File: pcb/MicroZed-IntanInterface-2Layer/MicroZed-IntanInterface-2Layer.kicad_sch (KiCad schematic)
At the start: 51 parts, among them J1 Screw_Terminal_01x02, J2 Conn_02x05_Odd_Even, J4 USB_C_Receptacle_USB2.0_16P, J7 GND header for probes, U1 AP331A, U2 TLV62568DDC, U9 TLV62568DDC

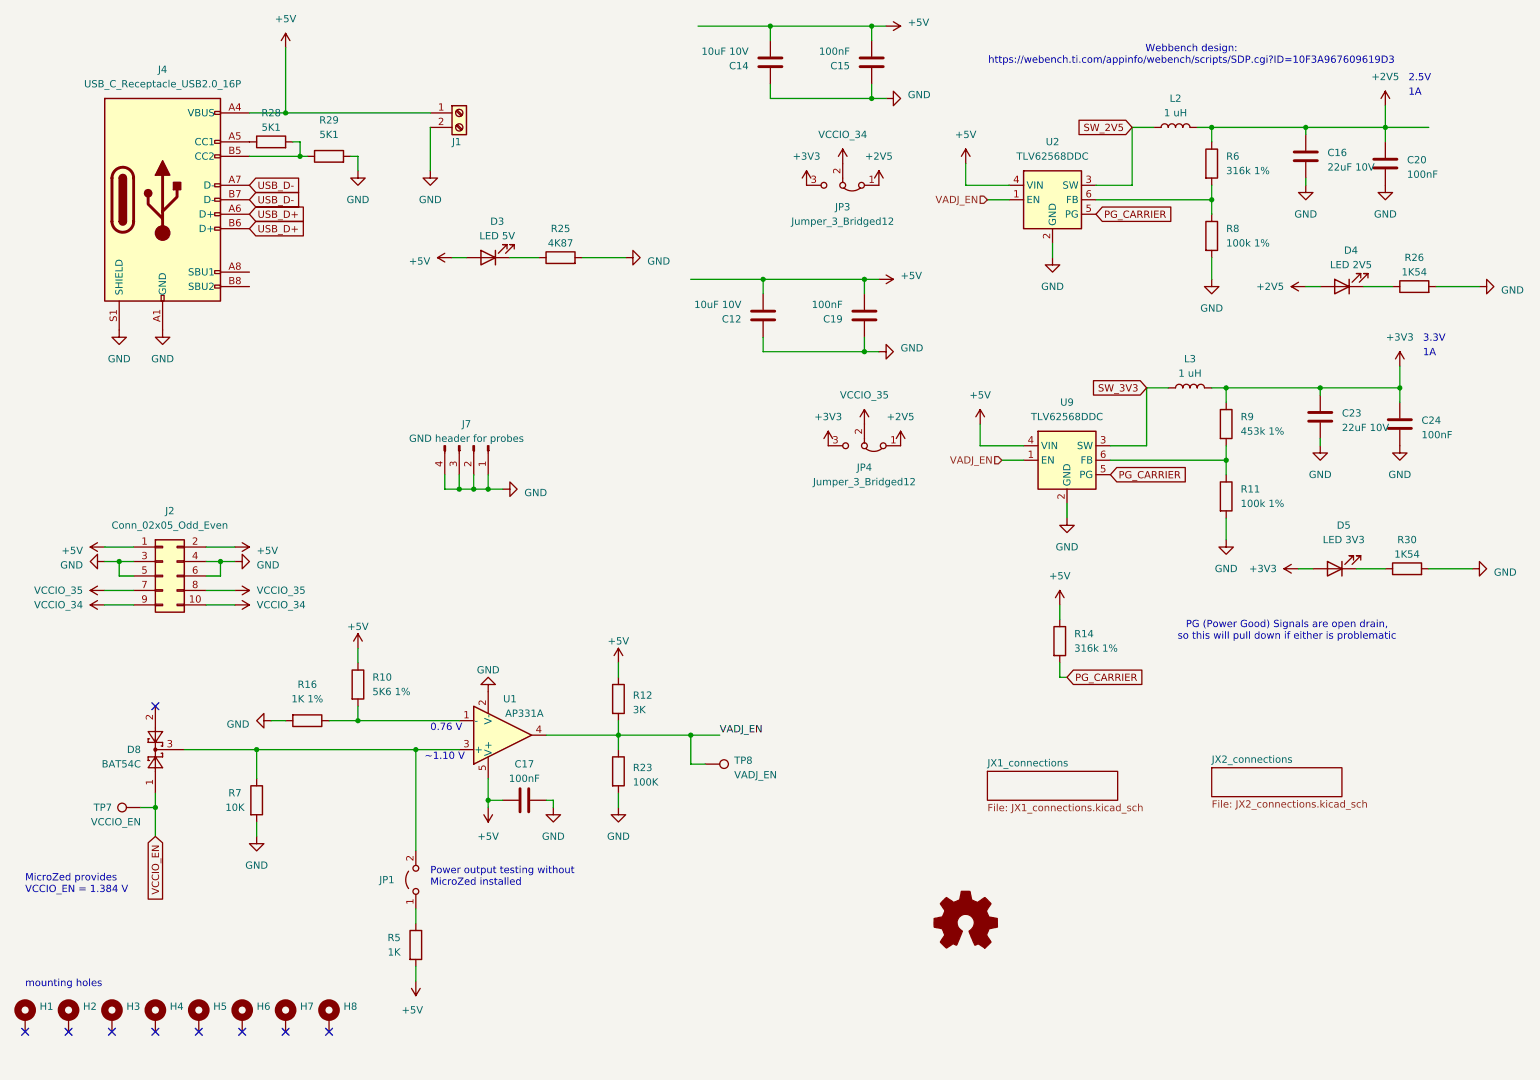
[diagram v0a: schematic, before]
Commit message: Updated PCB after v0.22 bug fixes
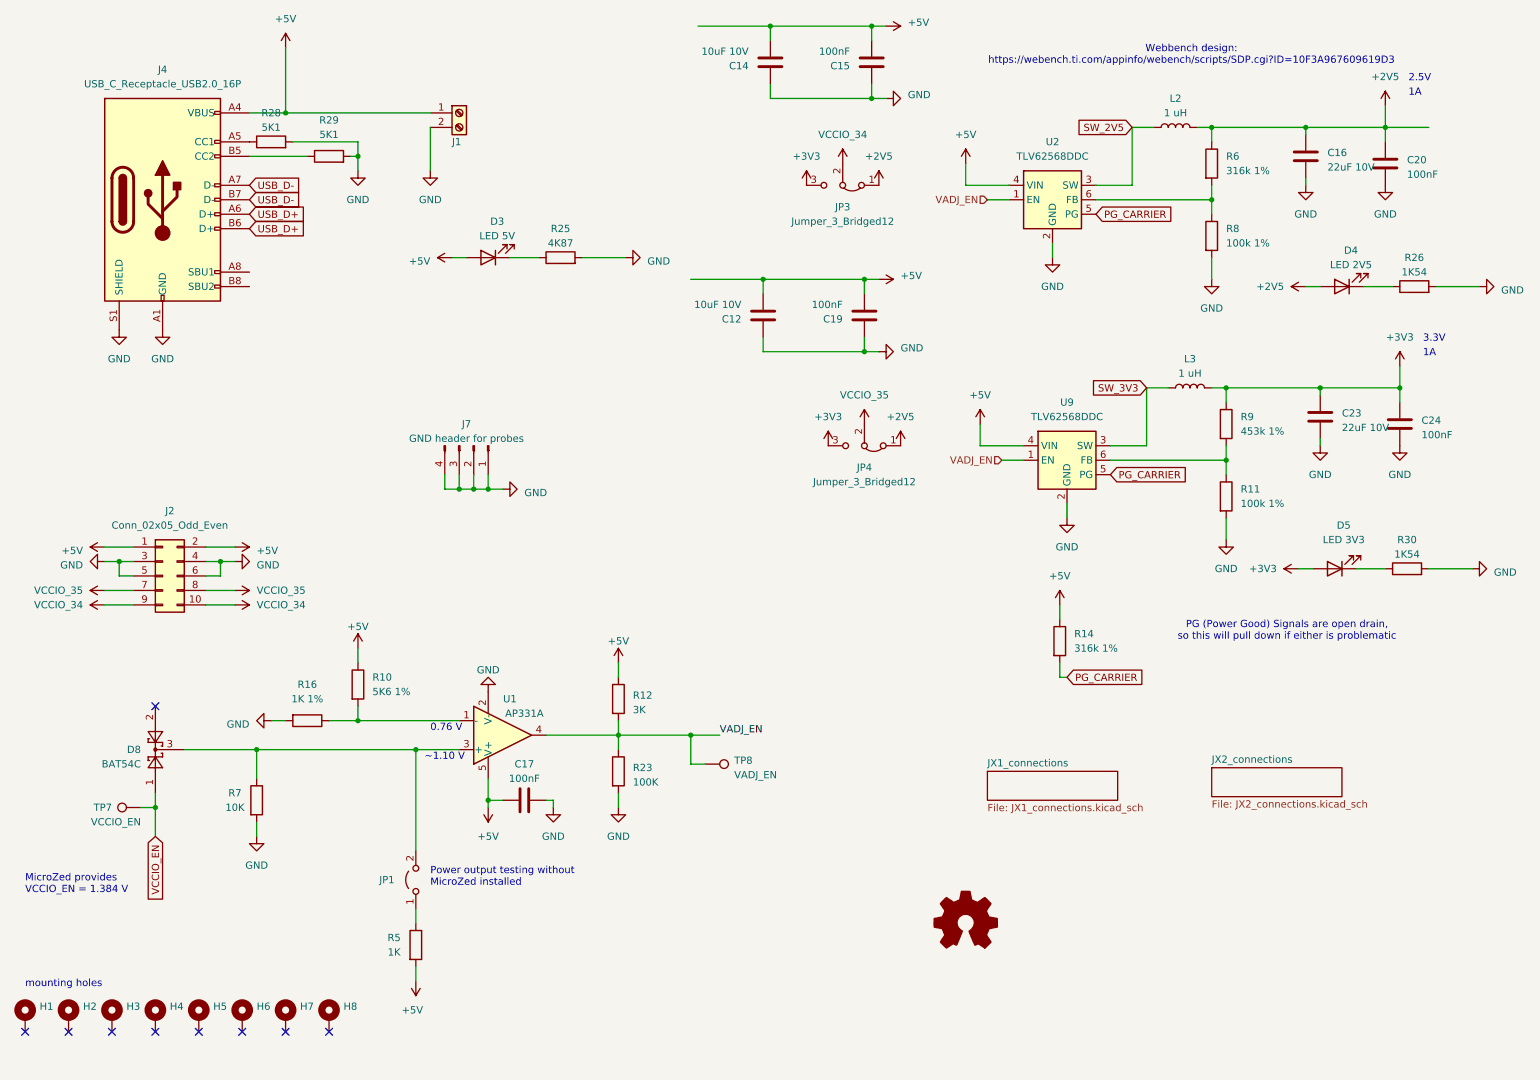
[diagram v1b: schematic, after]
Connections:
- net GND: now also R28.2
- net at J4.B5 (CC2), R29.1: no longer R28.2
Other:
- title: MicroZed development carrier board -> Intan Interface carrier board
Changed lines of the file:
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@@
 (kicad_sch
-	(version 20231120)
+	(version 20250114)
 	(generator "eeschema")
-	(generator_version "8.0")
+	(generator_version "9.0")
 	(paper "A4")
 	(title_block
-		(title "MicroZed development carrier board")
-		(date "2023-08-19")
-		(rev "4")
+		(title "Intan Interface carrier board")
+		(date "2025-08-18")
+		(rev "1.0")
 		(comment 1 "               License: Creative Commons Zero")
-		(comment 3 "               (c) 2023 Viktor Nikolov")
+		(comment 3 "               (c) 2025 Caleb Kemere")
+		(comment 4 "                    derived from a design by  Viktor Nikolov")
+	)
+	(text "1A"
+		(exclude_from_sim no)
+		(at 263.144 28.956 0)
+		(effects
+			(font
+				(size 1.27 1.27)
+			)
+			(justify left bottom)
+		)
+	)
+	(text "3.3V"
+		(exclude_from_sim no)
+		(at 265.684 72.136 0)
+		(effects
+			(font
+				(size 1.27 1.27)
+			)
+			(justify left bottom)
+		)
+	)
+	(text "mounting holes"
+		(exclude_from_sim no)
+		(at 20.32 185.42 0)
+		(effects
+			(font
+				(size 1.27 1.27)
+			)
+			(justify left bottom)
+		)
+	)
+	(text "2.5V"
+		(exclude_from_sim no)
+		(at 263.144 26.416 0)
+		(effects
+			(font
+				(size 1.27 1.27)
+			)
+			(justify left bottom)
+		)
+	)
+	(text "0.76 V"
+		(exclude_from_sim no)
+		(at 91.44 140.462 0)
+		(effects
+			(font
+				(size 1.27 1.27)
+			)
+			(justify left bottom)
+		)
+	)
+	(text "Webbench design:\nhttps://webench.ti.com/appinfo/webench/scripts/SDP.cgi?ID=10F3A967609619D3"
+		(exclude_from_sim no)
+		(at 225.044 21.59 0)
+		(effects
+			(font
+				(size 1.27 1.27)
+			)
+		)
+	)
+	(text "~1.10 V"
+		(exclude_from_sim no)
+		(at 90.424 145.542 0)
+		(effects
+			(font
+				(size 1.27 1.27)
+			)
+			(justify left bottom)
+		)
+	)
+	(text "Power output testing without\nMicroZed installed"
+		(exclude_from_sim no)
+		(at 91.44 167.64 0)
+		(effects
+			(font
+				(size 1.27 1.27)
+			)
+			(justify left bottom)
+		)
+	)
+	(text "1A"
+		(exclude_from_sim no)
+		(at 265.684 74.676 0)
+		(effects
+			(font
+				(size 1.27 1.27)
+			)
+			(justify left bottom)
+		)
+	)
+	(text "MicroZed provides\nVCCIO_EN = 1.384 V"
+		(exclude_from_sim no)
+		(at 20.32 168.91 0)
+		(effects
+			(font
+				(size 1.27 1.27)
+			)
+			(justify left bottom)
+		)
+	)
+	(text "PG (Power Good) Signals are open drain, \nso this will pull down if either is problematic\n"
+		(exclude_from_sim no)
+		(at 241.808 122.682 0)
+		(effects
+			(font
+				(size 1.27 1.27)
+			)
+		)
 	)
 	(junction
@@
 	)
 	(junction
+		(at 78.74 39.37)
+		(diameter 0)
+		(color 0 0 0 0)
+	)
+	(junction
 		(at 88.9 143.51)
 		(diameter 0)
@@
 	)
 	(junction
-		(at 68.58 39.37)
-		(diameter 0)
-		(color 0 0 0 0)
-	)
-	(junction
 		(at 259.08 34.29)
 		(diameter 0)
@@
 	(wire
 		(pts
-			(xy 68.58 36.83) (xy 68.58 39.37)
-		)
-		(stroke
-			(width 0)
-			(type default)
-		)
-	)
-	(wire
-		(pts
 			(xy 36.83 113.03) (xy 39.37 113.03)
 		)
@@
 	(wire
 		(pts
+			(xy 78.74 36.83) (xy 78.74 39.37)
+		)
+		(stroke
+			(width 0)
+			(type default)
+		)
+	)
+	(wire
+		(pts
 			(xy 171.45 29.21) (xy 168.91 29.21)
 		)
@@
 	(wire
 		(pts
-			(xy 67.31 36.83) (xy 68.58 36.83)
+			(xy 67.31 36.83) (xy 78.74 36.83)
 		)
 		(stroke
@@
 	(wire
 		(pts
-			(xy 69.85 39.37) (xy 68.58 39.37)
+			(xy 59.69 39.37) (xy 69.85 39.37)
 		)
 		(stroke
@@
 	(wire
 		(pts
-			(xy 68.58 39.37) (xy 59.69 39.37)
-		)
-		(stroke
-			(width 0)
-			(type default)
-		)
-	)
-	(wire
-		(pts
 			(xy 228.6 60.96) (xy 228.6 57.15)
 		)
@@
 		)
 	)
-	(text "1A"
-		(exclude_from_sim no)
-		(at 263.144 28.956 0)
-		(effects
-			(font
-				(size 1.27 1.27)
-			)
-			(justify left bottom)
-		)
-	)
-	(text "3.3V"
-		(exclude_from_sim no)
-		(at 265.684 72.136 0)
-		(effects
-			(font
-				(size 1.27 1.27)
-			)
-			(justify left bottom)
-		)
-	)
-	(text "mounting holes"
-		(exclude_from_sim no)
-		(at 20.32 185.42 0)
-		(effects
-			(font
-				(size 1.27 1.27)
-			)
-			(justify left bottom)
-		)
-	)
-	(text "2.5V"
-		(exclude_from_sim no)
-		(at 263.144 26.416 0)
-		(effects
-			(font
-				(size 1.27 1.27)
-			)
-			(justify left bottom)
-		)
-	)
-	(text "0.76 V"
-		(exclude_from_sim no)
-		(at 91.44 140.462 0)
-		(effects
-			(font
-				(size 1.27 1.27)
-			)
-			(justify left bottom)
-		)
-	)
-	(text "Webbench design:\nhttps://webench.ti.com/appinfo/webench/scripts/SDP.cgi?ID=10F3A967609619D3"
-		(exclude_from_sim no)
-		(at 225.044 21.59 0)
-		(effects
-			(font
-				(size 1.27 1.27)
-			)
-		)
-	)
-	(text "~1.10 V"
-		(exclude_from_sim no)
-		(at 90.424 145.542 0)
-		(effects
-			(font
-				(size 1.27 1.27)
-			)
-			(justify left bottom)
-		)
-	)
-	(text "Power output testing without\nMicroZed installed"
-		(exclude_from_sim no)
-		(at 91.44 167.64 0)
-		(effects
-			(font
-				(size 1.27 1.27)
-			)
-			(justify left bottom)
-		)
-	)
-	(text "1A"
-		(exclude_from_sim no)
-		(at 265.684 74.676 0)
-		(effects
-			(font
-				(size 1.27 1.27)
-			)
-			(justify left bottom)
-		)
-	)
-	(text "MicroZed provides\nVCCIO_EN = 1.384 V"
-		(exclude_from_sim no)
-		(at 20.32 168.91 0)
-		(effects
-			(font
-				(size 1.27 1.27)
-			)
-			(justify left bottom)
-		)
-	)
-	(text "PG (Power Good) Signals are open drain, \nso this will pull down if either is problematic\n"
-		(exclude_from_sim no)
-		(at 241.808 122.682 0)
-		(effects
-			(font
-				(size 1.27 1.27)
-			)
-		)
-	)
 	(label "VADJ_EN"
 		(at 142.24 140.97 0)
@@
 		(at 189.23 147.32)
 		(size 22.86 5.08)
+		(exclude_from_sim no)
+		(in_bom yes)
+		(on_board yes)
+		(dnp no)
 		(fields_autoplaced yes)
 		(stroke
@@
 		)
 		(instances
-			(project "MicroZed-IntanInterface"
+			(project "MicroZed-IntanInterface-2Layer"
 				(path "/e2973d32-f02d-4cac-9cf4-7229e04d7d6c"
 					(page "2")
@@
 		(at 228.6 146.685)
 		(size 22.86 5.08)
+		(exclude_from_sim no)
+		(in_bom yes)
+		(on_board yes)
+		(dnp no)
 		(fields_autoplaced yes)
 		(stroke
@@
 		)
 		(instances
-			(project "MicroZed-IntanInterface"
+			(project "MicroZed-IntanInterface-2Layer"
 				(path "/e2973d32-f02d-4cac-9cf4-7229e04d7d6c"
 					(page "3")
@@
 		)
 	)
+	(embedded_fonts no)
 )

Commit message: Updates for version 1.0 to ship to UMich
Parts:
- removed JP1: Jumper_2_Open, Connector_PinHeader_2.54mm:PinHeader_1x02_P2.54mm_Vertical, symbol Jumper:Jumper_2_Open
- removed JP3, JP4: Jumper_3_Bridged12, Connector_PinHeader_2.54mm:PinHeader_1x03_P2.54mm_Vertical, symbol Jumper:Jumper_3_Bridged12
- added JP5: SolderJumper_2_Open, Jumper:SolderJumper-2_P1.3mm_Open_RoundedPad1.0x1.5mm, symbol Jumper:SolderJumper_2_Open
- added SW3, SW4: SW_SPDT, Button_Switch_SMD:SW_SPDT_PCM12, symbol Switch:SW_SPDT
- C15, C17, C19, C20, C24: footprint Capacitor_SMD:C_0603_1608Metric -> Capacitor_SMD:C_0402_1005Metric; LCSC C66501 -> C307331
- C16, C23: value 22uF 10V -> 22uF 25V; LCSC C5672 -> C12891
- D3, D4, D5: LCSC C2833058 -> C2286
- H1, H2, H3, H4, H5, H6, H7, H8: footprint Viktor:MountingHole_3.2mm_Pad_7mm -> MountingHole:MountingHole_3.2mm_M3_Pad
- J2: now not fitted; now left out of the parts list
- J4: LCSC (none) -> C5184243
- L2, L3: footprint Inductor_SMD:L_1008_2520Metric -> Inductor_SMD:L_1210_3225Metric; LCSC (none) -> C47492669
- R10: value 5K6 1% -> 5.6k 1%; footprint Resistor_SMD:R_0603_1608Metric -> Resistor_SMD:R_0402_1005Metric; LCSC C22843 -> C25908
- R11, R8: footprint Resistor_SMD:R_0603_1608Metric -> Resistor_SMD:R_0402_1005Metric; LCSC (none) -> C25741
- R12: value 3K -> 3k; footprint Resistor_SMD:R_0603_1608Metric -> Resistor_SMD:R_0402_1005Metric; LCSC C4211 -> C22978
- R14, R6: footprint Resistor_SMD:R_0603_1608Metric -> Resistor_SMD:R_0402_1005Metric; LCSC (none) -> C4338094
- R16: value 1K 1% -> 1k 1%; footprint Resistor_SMD:R_0603_1608Metric -> Resistor_SMD:R_0402_1005Metric; LCSC C23228 -> C11702
- R23: value 100K -> 100k 1%; footprint Resistor_SMD:R_0603_1608Metric -> Resistor_SMD:R_0402_1005Metric; LCSC C25803 -> C25741
- R25: value 4K87 -> 1k 1%; footprint Resistor_SMD:R_0603_1608Metric -> Resistor_SMD:R_0402_1005Metric; LCSC C2097544 -> C11702
- R26, R30: value 1K54 -> 1k 1%; footprint Resistor_SMD:R_0603_1608Metric -> Resistor_SMD:R_0402_1005Metric; LCSC C100784 -> C11702
- R28, R29: value 5K1 -> 5.1k; footprint Resistor_SMD:R_0603_1608Metric -> Resistor_SMD:R_0402_1005Metric; LCSC C2097544 -> C25905
- R5: value 1K -> 1k 1%; footprint Resistor_SMD:R_0603_1608Metric -> Resistor_SMD:R_0402_1005Metric; LCSC C21190 -> C11702
- R7: value 10K -> 10k; footprint Resistor_SMD:R_0603_1608Metric -> Resistor_SMD:R_0402_1005Metric; LCSC C25804 -> C25744
- R9: footprint Resistor_SMD:R_0603_1608Metric -> Resistor_SMD:R_0402_1005Metric; LCSC (none) -> C3025678
- TP7, TP8: footprint Viktor:TestPoint__Drill1.0mm -> TestPoint:TestPoint_THTPad_D2.0mm_Drill1.0mm
- U2, U9: value TLV62568DDC -> TLV62568PDRLR; footprint Package_TO_SOT_SMD:SOT-23-6 -> Package_TO_SOT_SMD:SOT-563; LCSC (none) -> C398368
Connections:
- net +2V5: now also SW3.1 (A), SW4.1 (A)
- net +3V3: now also SW3.3 (C), SW4.3 (C)
- net GND: now also H1.1, H2.1, H3.1, H4.1, H5.1, H6.1, H7.1, H8.1
- net VCCIO_34: now also SW3.2 (B)
- net VCCIO_35: now also SW4.2 (B)
- net at D8.3, R7.1, U1.3 (+): now also JP5.1 (A)
- net at R5.1: now also JP5.2 (B)
- no-connect marks 9 -> 1
